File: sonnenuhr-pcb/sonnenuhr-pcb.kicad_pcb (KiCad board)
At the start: 2 copper layers, 5 parts, among them J1 Conn_01x05_Male, J2 Conn_01x05_Male, U1 ULN2803A

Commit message: sonnenuhr-pcb: add capacitors
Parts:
- added C1: 100nF, Capacitor_SMD:C_0805_2012Metric, F.Cu at (54.6, 63.5)
- added C2: 100uF, Capacitor_THT:CP_Radial_D5.0mm_P2.00mm, F.Cu at (54.0, 68.6)
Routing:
- net +5V: track 66.6 -> 73.3 mm
- net Net-(J2-Pad1): track 7.25 -> 6.35 mm

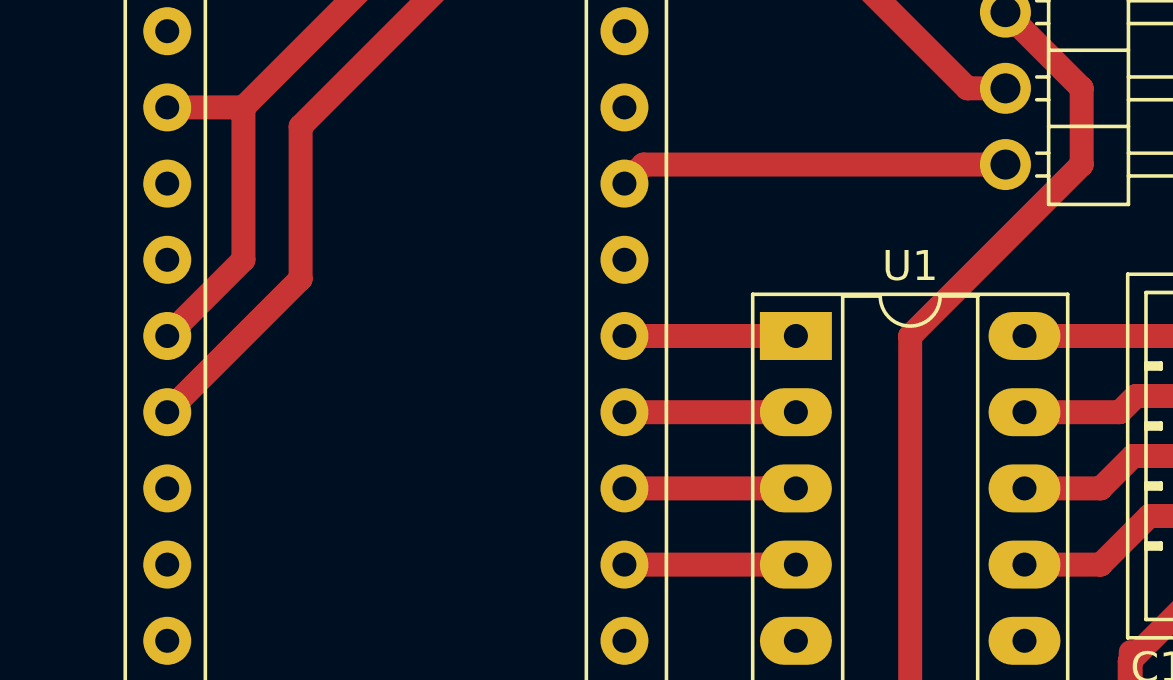
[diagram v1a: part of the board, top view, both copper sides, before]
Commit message: sonnenuhr-pcb: Add potentiometer
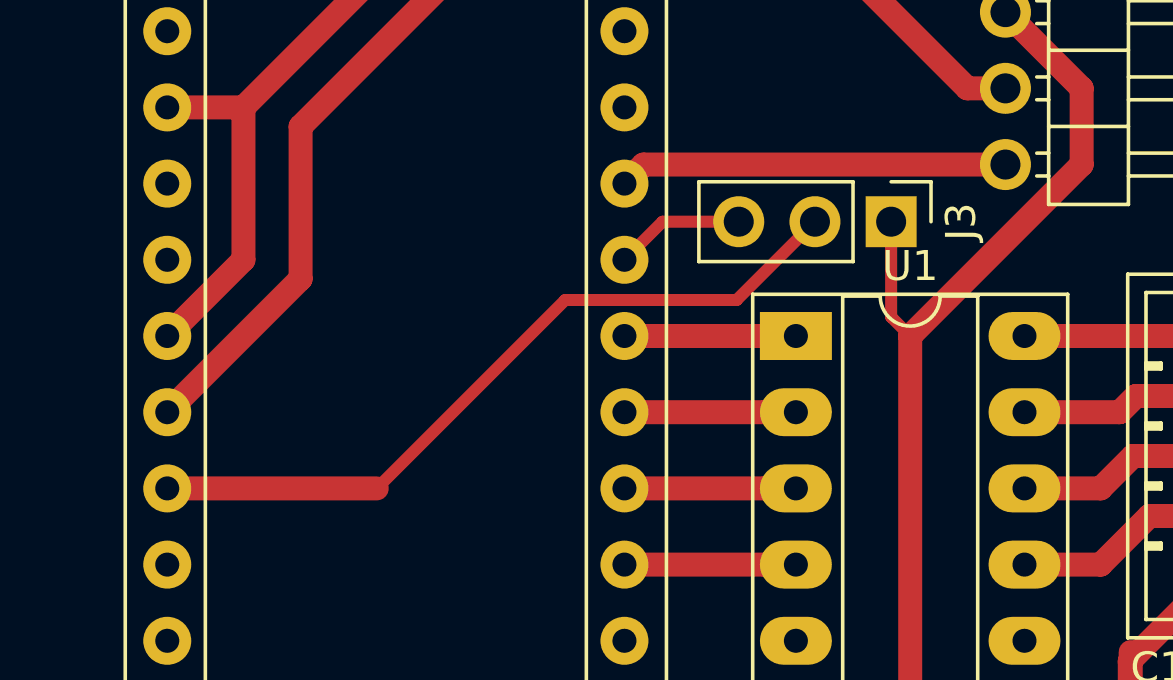
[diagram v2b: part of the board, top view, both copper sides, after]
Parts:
- added J3: Conn_01x03_Male, Connector_PinHeader_2.54mm:PinHeader_1x03_P2.54mm_Vertical, F.Cu at (45.7, 47.0)
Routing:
- net Net-(A1-Pad22): track 0.00 -> 25.3 mm
- net Net-(A1-Pad12): track 0.00 -> 4.34 mm
- net GND: track 62.0 -> 66.1 mm
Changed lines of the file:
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@@
     (thickness 1.6)
     (drawings 5)
-    (tracks 69)
+    (tracks 77)
     (zones 0)
-    (modules 7)
+    (modules 8)
     (nets 43)
   )
@@
   )
   (setup
-    (last_trace_width 0.8)
+    (last_trace_width 0.4)
     (user_trace_width 0.8)
     (trace_clearance 0.2)
@@
     (add_net "Net-(U1-Pad7)")
     (add_net "Net-(U1-Pad8)")
+  )
+  (module Connector_PinHeader_2.54mm:PinHeader_1x03_P2.54mm_Vertical (layer F.Cu)
+    (at 45.72 46.99 270)
+    (descr "Through hole straight pin header, 1x03, 2.54mm pitch, single row")
+    (tags "Through hole pin header THT 1x03 2.54mm single row")
+    (fp_text reference J3 (at 0 -2.33 90) (layer F.SilkS)
+      (effects (font (size 1 1) (thickness 0.15)))
+    )
+    (fp_text value Conn_01x03_Male (at 0 7.41 90) (layer F.Fab)
+      (effects (font (size 1 1) (thickness 0.15)))
+    )
+    (fp_text user %R (at 0 2.54) (layer F.Fab)
+      (effects (font (size 1 1) (thickness 0.15)))
+    )
+    (fp_line (start 1.8 -1.8) (end -1.8 -1.8) (layer F.CrtYd) (width 0.05))
+    (fp_line (start 1.8 6.85) (end 1.8 -1.8) (layer F.CrtYd) (width 0.05))
+    (fp_line (start -1.8 6.85) (end 1.8 6.85) (layer F.CrtYd) (width 0.05))
+    (fp_line (start -1.8 -1.8) (end -1.8 6.85) (layer F.CrtYd) (width 0.05))
+    (fp_line (start -1.33 -1.33) (end 0 -1.33) (layer F.SilkS) (width 0.12))
+    (fp_line (start -1.33 0) (end -1.33 -1.33) (layer F.SilkS) (width 0.12))
+    (fp_line (start -1.33 1.27) (end 1.33 1.27) (layer F.SilkS) (width 0.12))
+    (fp_line (start 1.33 1.27) (end 1.33 6.41) (layer F.SilkS) (width 0.12))
+    (fp_line (start -1.33 1.27) (end -1.33 6.41) (layer F.SilkS) (width 0.12))
+    (fp_line (start -1.33 6.41) (end 1.33 6.41) (layer F.SilkS) (width 0.12))
+    (fp_line (start -1.27 -0.635) (end -0.635 -1.27) (layer F.Fab) (width 0.1))
+    (fp_line (start -1.27 6.35) (end -1.27 -0.635) (layer F.Fab) (width 0.1))
+    (fp_line (start 1.27 6.35) (end -1.27 6.35) (layer F.Fab) (width 0.1))
+    (fp_line (start 1.27 -1.27) (end 1.27 6.35) (layer F.Fab) (width 0.1))
+    (fp_line (start -0.635 -1.27) (end 1.27 -1.27) (layer F.Fab) (width 0.1))
+    (pad 3 thru_hole oval (at 0 5.08 270) (size 1.7 1.7) (drill 1) (layers *.Cu *.Mask)
+      (net 7 "Net-(A1-Pad12)"))
+    (pad 2 thru_hole oval (at 0 2.54 270) (size 1.7 1.7) (drill 1) (layers *.Cu *.Mask)
+      (net 18 "Net-(A1-Pad22)"))
+    (pad 1 thru_hole rect (at 0 0 270) (size 1.7 1.7) (drill 1) (layers *.Cu *.Mask)
+      (net 5 GND))
+    (model ${KISYS3DMOD}/Connector_PinHeader_2.54mm.3dshapes/PinHeader_1x03_P2.54mm_Vertical.wrl
+      (at (xyz 0 0 0))
+      (scale (xyz 1 1 1))
+      (rotate (xyz 0 0 0))
+    )
   )
   (module Capacitor_THT:CP_Radial_D5.0mm_P2.00mm (layer F.Cu)
@@
   (segment (start 21.59 73.66) (end 30.48 73.66) (width 0.8) (layer F.Cu) (net 5))
   (segment (start 30.48 73.66) (end 35.56 68.58) (width 0.8) (layer F.Cu) (net 5))
+  (segment (start 45.72 50.165) (end 46.355 50.8) (width 0.4) (layer F.Cu) (net 5))
+  (segment (start 45.72 46.99) (end 45.72 50.165) (width 0.4) (layer F.Cu) (net 5))
+  (segment (start 38.1 46.99) (end 36.83 48.26) (width 0.4) (layer F.Cu) (net 7))
+  (segment (start 40.64 46.99) (end 38.1 46.99) (width 0.4) (layer F.Cu) (net 7))
   (segment (start 18.415 70.485) (end 20.32 68.58) (width 0.8) (layer F.Cu) (net 8))
   (segment (start 18.415 77.47) (end 18.415 70.485) (width 0.8) (layer F.Cu) (net 8))
@@
   (segment (start 41.51 58.42) (end 41.91 58.42) (width 0.8) (layer F.Cu) (net 15) (status 30))
   (segment (start 36.83 58.42) (end 42.545 58.42) (width 0.8) (layer F.Cu) (net 15) (status 30))
+  (segment (start 21.59 55.88) (end 28.575 55.88) (width 0.8) (layer F.Cu) (net 18))
+  (segment (start 34.855001 49.599999) (end 28.575 55.88) (width 0.4) (layer F.Cu) (net 18))
+  (segment (start 40.570001 49.599999) (end 34.855001 49.599999) (width 0.4) (layer F.Cu) (net 18))
+  (segment (start 43.18 46.99) (end 40.570001 49.599999) (width 0.4) (layer F.Cu) (net 18))
   (segment (start 31.75 37.465) (end 29.845 37.465) (width 0.8) (layer F.Cu) (net 21))
   (segment (start 31.75 37.465) (end 30.48 37.465) (width 0.8) (layer F.Cu) (net 21))
